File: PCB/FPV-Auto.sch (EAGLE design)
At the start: 93 parts, among them Q310 CSD25402Q3A, Q320 BSS138, U110 NRF24L01+_MINI, U120 74LVC2T45DCT, U140 DRV8835, U200 RASPBERRY_PI_ZERO_W_V1.1_GPIO, U210 MAX98357A, U300 BQ25892, U330 TPS61236P, U340 TPS61236P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

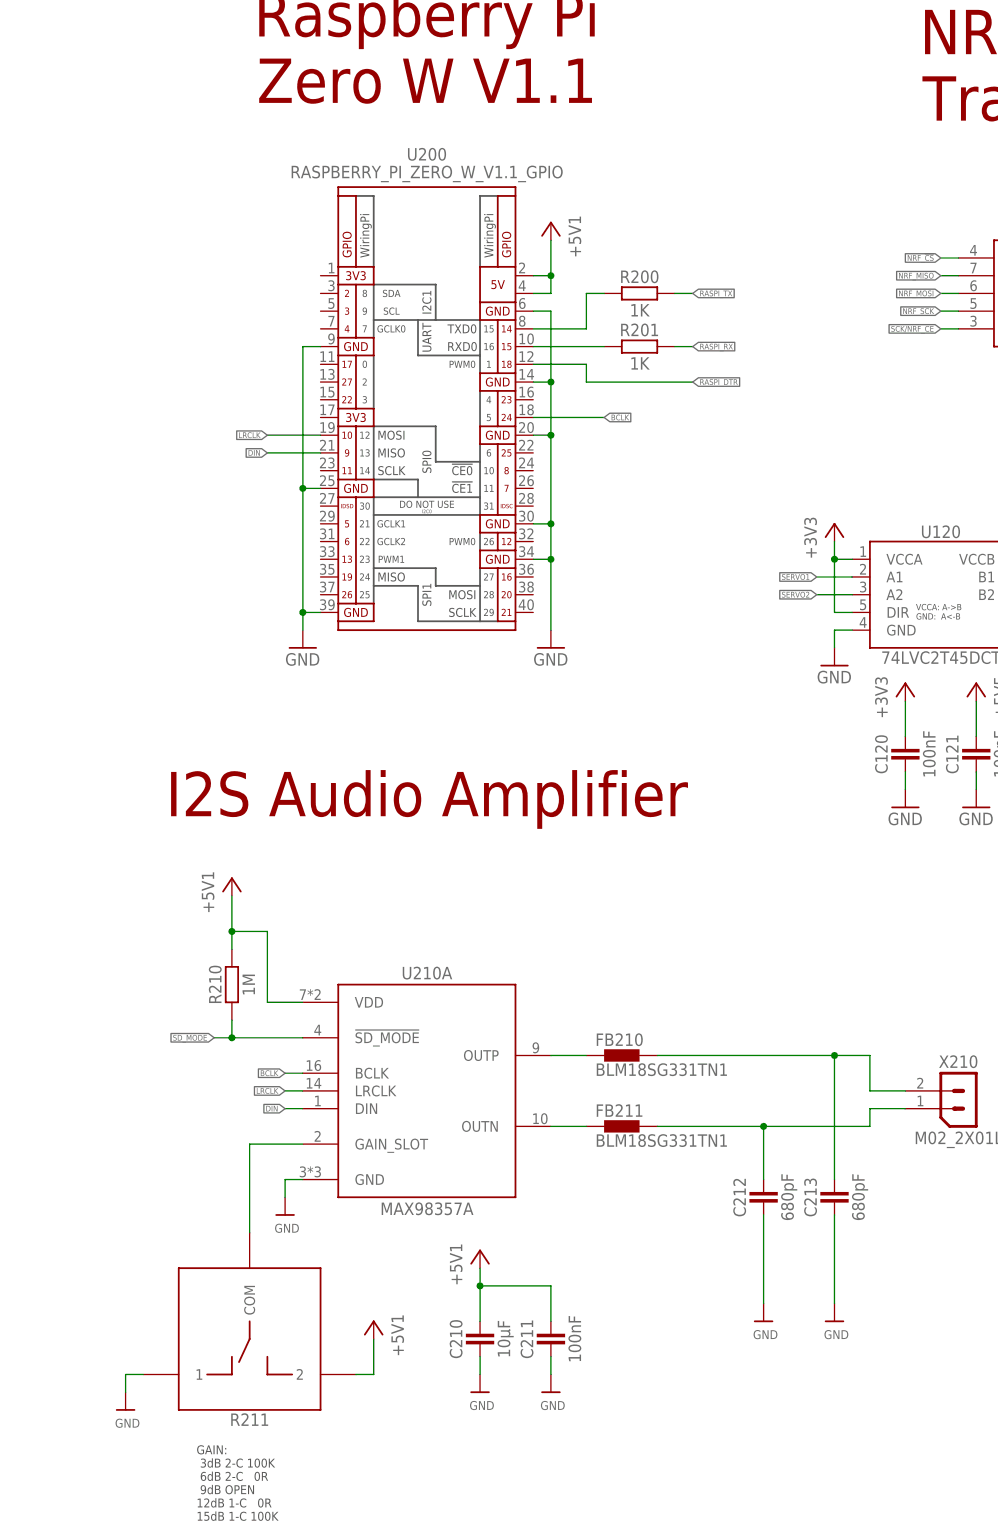
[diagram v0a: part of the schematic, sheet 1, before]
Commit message: Changes on Raspberry GPIO assignment
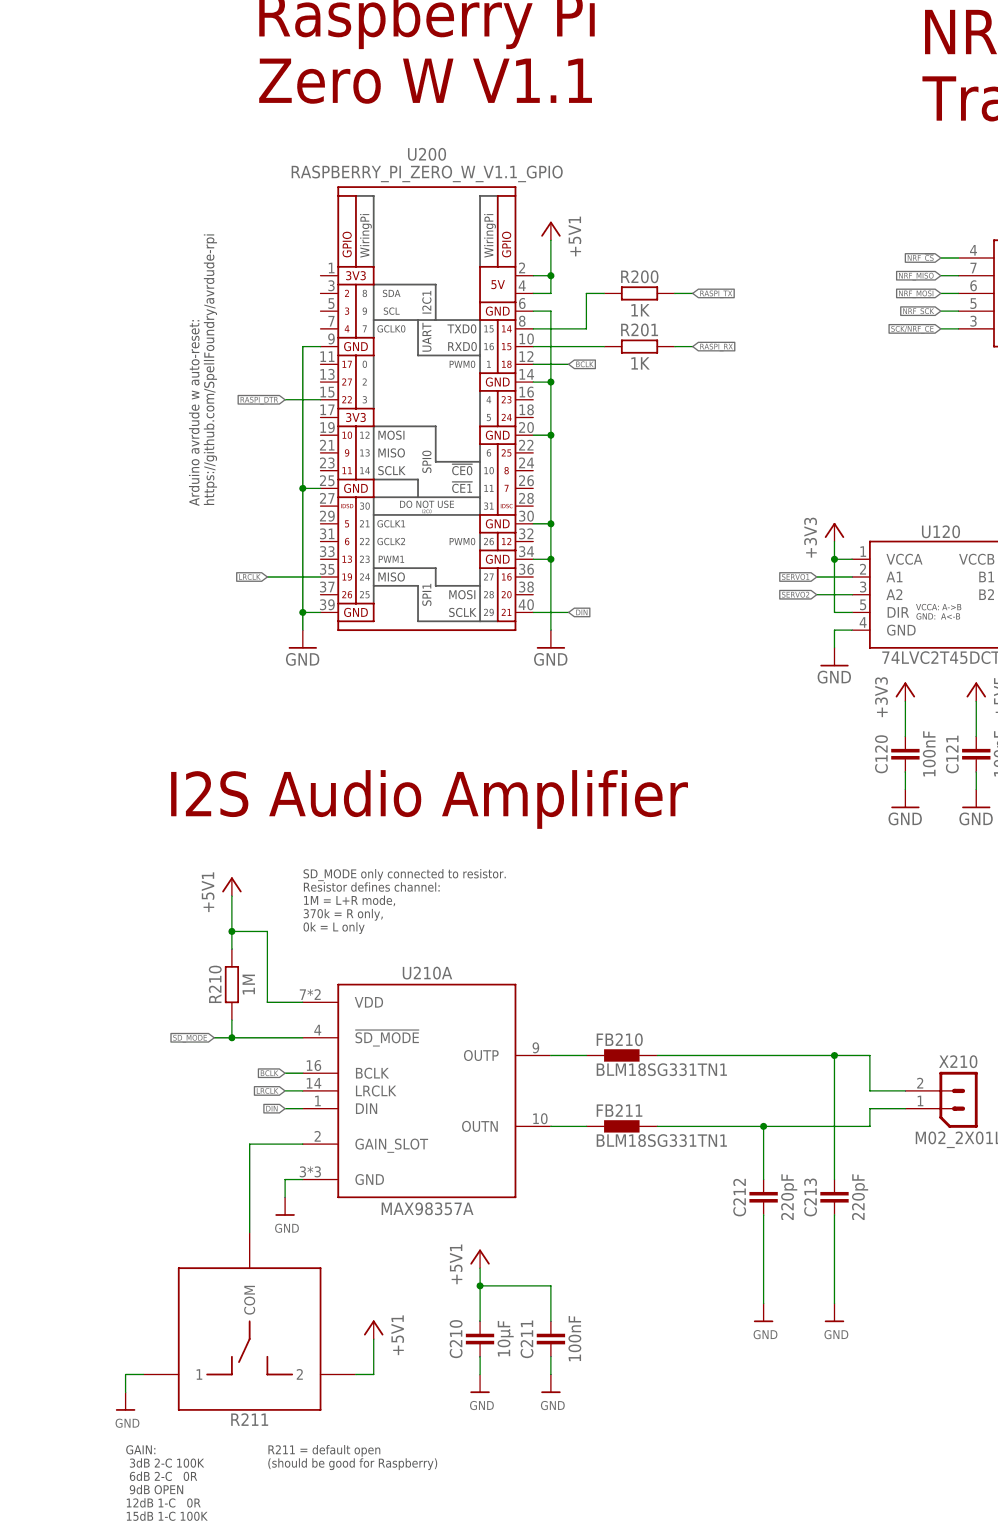
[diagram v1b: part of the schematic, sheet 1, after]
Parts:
- C212, C213: value 680pF -> 220pF
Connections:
- net BCLK: now also U200.GPIO18; no longer U200.GPIO24/GEN5
- net DIN: now also U200.GPIO21; no longer U200.GPIO9/MISO
- net LRCLK: now also U200.GPIO19; no longer U200.GPIO10/MOSI
- net RASPI_DTR: now also U200.GPIO22/GEN3; no longer U200.GPIO18
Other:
- note added: "Arduino avrdude w auto-reset: https://github.com/SpellFoundry/avrdude-rpi"
- note added: "DIN, BCLK, LRCLK was on wrong pins (was pin# instead GPIO#). Should be now: DIN=GPIO21, BLCK=GPIO18, LRCLK=GPIO19"
- note added: "R211 = default open (should be good for Raspberry)"
- note added: "SD_MODE only connected to resistor. Resistor defines channel: 1M = L+R mode, 370k = R only, 0k = L only"
- note added: "Yes please, this is better for antenna"
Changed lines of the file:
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@@
 <layer number="250" name="Descript" color="7" fill="1" visible="yes" active="yes"/>
 <layer number="251" name="SMDround" color="7" fill="1" visible="yes" active="yes"/>
-<layer number="254" name="Kommentar" color="7" fill="1" visible="yes" active="yes"/>
+<layer number="254" name="Kommentar" color="12" fill="1" visible="yes" active="yes"/>
 <layer number="255" name="HELP" color="7" fill="1" visible="yes" active="yes"/>
 </layers>
@@
 <part name="R200" library="FPV-Auto" deviceset="R" device="" value="1K"/>
 <part name="R201" library="FPV-Auto" deviceset="R" device="" value="1K"/>
-<part name="C212" library="FPV-Auto" deviceset="C" device="0603" value="680pF"/>
-<part name="C213" library="FPV-Auto" deviceset="C" device="0603" value="680pF"/>
+<part name="C212" library="FPV-Auto" deviceset="C" device="0603" value="220pF"/>
+<part name="C213" library="FPV-Auto" deviceset="C" device="0603" value="220pF"/>
 <part name="R211" library="FPV-Auto" deviceset="R_SWITCH_2_WAY" device="_0603" value="R_SWITCH_2_WAY_0603"/>
 <part name="+5V7" library="FPV-Auto" deviceset="+5V1" device=""/>
@@
 Zero W V1.1</text>
 <text x="101.6" y="228.6" size="6.35" layer="94" rot="R180" align="bottom-center">ATmega328/P</text>
-<text x="193.04" y="20.32" size="1.27" layer="97" align="top-left">GAIN:
+<text x="182.88" y="20.32" size="1.27" layer="97" align="top-left">GAIN:
  3dB 2-C 100K
  6dB 2-C   0R
@@
 <text x="166.116" y="152.654" size="1.778" layer="150" align="center-left">pin changed</text>
 <text x="166.116" y="139.954" size="1.778" layer="150" align="center-left">pin changed</text>
+<text x="195.58" y="127" size="1.27" layer="254">DIN, BCLK, LRCLK was on wrong pins (was pin# instead GPIO#).
+Should be now: DIN=GPIO21, BLCK=GPIO18, LRCLK=GPIO19</text>
+<text x="208.28" y="93.98" size="1.27" layer="97">SD_MODE only connected to resistor.
+Resistor defines channel:
+1M = L+R mode,
+370k = R only,
+0k = L only</text>
+<text x="203.2" y="20.32" size="1.27" layer="97" align="top-left">R211 = default open
+(should be good for Raspberry)</text>
+<text x="337.82" y="198.12" size="1.778" layer="254">Yes please, this is
+better for antenna </text>
+<text x="195.58" y="154.94" size="1.4224" layer="97" rot="R90">Arduino avrdude w auto-reset:
+https://github.com/SpellFoundry/avrdude-rpi</text>
 </plain>
 <instances>
@@
 </segment>
 <segment>
-<pinref part="U200" gate="GPIO" pin="GPIO24/GEN5"/>
-<wire x1="241.3" y1="167.64" x2="251.46" y2="167.64" width="0.1524" layer="91"/>
-<label x="251.46" y="167.64" size="0.8128" layer="95" xref="yes"/>
+<label x="246.38" y="175.26" size="0.8128" layer="95" xref="yes"/>
+<pinref part="U200" gate="GPIO" pin="GPIO18"/>
+<wire x1="246.38" y1="175.26" x2="241.3" y2="175.26" width="0.1524" layer="91"/>
 </segment>
 </net>
@@
 </segment>
 <segment>
-<pinref part="U200" gate="GPIO" pin="GPIO10/MOSI"/>
-<wire x1="210.82" y1="165.1" x2="203.2" y2="165.1" width="0.1524" layer="91"/>
-<label x="203.2" y="165.1" size="0.8128" layer="95" rot="R180" xref="yes"/>
+<label x="203.2" y="144.78" size="0.8128" layer="95" rot="R180" xref="yes"/>
+<pinref part="U200" gate="GPIO" pin="GPIO19"/>
+<wire x1="210.82" y1="144.78" x2="203.2" y2="144.78" width="0.1524" layer="91"/>
 </segment>
 </net>
@@
 </segment>
 <segment>
-<pinref part="U200" gate="GPIO" pin="GPIO9/MISO"/>
-<wire x1="210.82" y1="162.56" x2="203.2" y2="162.56" width="0.1524" layer="91"/>
-<label x="203.2" y="162.56" size="0.8128" layer="95" rot="R180" xref="yes"/>
+<label x="246.38" y="139.7" size="0.8128" layer="95" xref="yes"/>
+<pinref part="U200" gate="GPIO" pin="GPIO21"/>
+<wire x1="241.3" y1="139.7" x2="246.38" y2="139.7" width="0.1524" layer="91"/>
 </segment>
 </net>
@@
 <net name="RASPI_DTR" class="0">
 <segment>
-<pinref part="U200" gate="GPIO" pin="GPIO18"/>
-<wire x1="241.3" y1="175.26" x2="248.92" y2="175.26" width="0.1524" layer="91"/>
-<wire x1="248.92" y1="175.26" x2="248.92" y2="172.72" width="0.1524" layer="91"/>
-<wire x1="248.92" y1="172.72" x2="264.16" y2="172.72" width="0.1524" layer="91"/>
-<label x="264.16" y="172.72" size="0.8128" layer="95" xref="yes"/>
-</segment>
-<segment>
+<label x="205.74" y="170.18" size="0.8128" layer="95" rot="R180" xref="yes"/>
+<pinref part="U200" gate="GPIO" pin="GPIO22/GEN3"/>
+<wire x1="210.82" y1="170.18" x2="205.74" y2="170.18" width="0.1524" layer="91"/>
+</segment>
+<segment>

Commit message: Update PCB Layout
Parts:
- added R101: 10K, FPV-Auto:R
- added R103: 1K, FPV-Auto:R
- R102: value 10K -> 1K
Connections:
- net +3V3: now also R101.2, R103.2
- net RESET: now also R101.1; no longer R102.1
- net SCL: now also R103.1
- net SDA: now also R102.1
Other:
- note added: "pin 9 connected to GND"
- moved on the sheet: R102, U110
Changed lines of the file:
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@@
 <part name="+3V2" library="supply1" deviceset="+3V3" device=""/>
 <part name="+3V3" library="supply1" deviceset="+3V3" device=""/>
-<part name="R102" library="FPV-Auto" deviceset="R" device="" value="10K"/>
+<part name="R101" library="FPV-Auto" deviceset="R" device="" value="10K"/>
 <part name="C104" library="FPV-Auto" deviceset="C" device="0603" value="100nF"/>
 <part name="R304" library="FPV-Auto" deviceset="R" device="" value="30K1"/>
@@
 <part name="GND40" library="supply1" deviceset="GND" device=""/>
 <part name="GND41" library="supply1" deviceset="GND" device=""/>
+<part name="R103" library="FPV-Auto" deviceset="R" device="" value="1K"/>
+<part name="R102" library="FPV-Auto" deviceset="R" device="" value="1K"/>
+<part name="+3V4" library="supply1" deviceset="+3V3" device=""/>
 </parts>
 <sheets>
@@
 <text x="195.58" y="154.94" size="1.4224" layer="97" rot="R90">Arduino avrdude w auto-reset:
 https://github.com/SpellFoundry/avrdude-rpi</text>
+<text x="305.816" y="205.994" size="1.778" layer="150" align="center-left">pin 9 connected to GND</text>
 </plain>
 <instances>
@@
 <instance part="+3V2" gate="G$1" x="48.26" y="215.9"/>
 <instance part="+3V3" gate="G$1" x="17.78" y="208.28"/>
-<instance part="R102" gate="A" x="48.26" y="205.74" smashed="yes" rot="R90">
+<instance part="R101" gate="A" x="48.26" y="205.74" smashed="yes" rot="R90">
 <attribute name="NAME" x="46.7614" y="205.74" size="1.778" layer="95" font="vector" rot="R90" align="bottom-center"/>
 <attribute name="VALUE" x="49.784" y="205.74" size="1.778" layer="96" font="vector" rot="R90" align="top-center"/>
@@
 <instance part="C120" gate="A" x="294.64" y="119.38"/>
 <instance part="C121" gate="A" x="304.8" y="119.38"/>
+<instance part="R103" gate="A" x="175.26" y="195.58" smashed="yes" rot="R90">
+<attribute name="NAME" x="173.7614" y="195.58" size="1.778" layer="95" font="vector" rot="R90" align="bottom-center"/>
+<attribute name="VALUE" x="176.784" y="195.58" size="1.778" layer="96" font="vector" rot="R90" align="top-center"/>
+</instance>
+<instance part="R102" gate="A" x="167.64" y="195.58" smashed="yes" rot="R90">
+<attribute name="NAME" x="166.1414" y="195.58" size="1.778" layer="95" font="vector" rot="R90" align="bottom-center"/>
+<attribute name="VALUE" x="169.164" y="195.58" size="1.778" layer="96" font="vector" rot="R90" align="top-center"/>
+</instance>
+<instance part="+3V4" gate="G$1" x="175.26" y="210.82"/>
 </instances>
 <busses>
@@
 <wire x1="48.26" y1="213.36" x2="48.26" y2="210.82" width="0.1524" layer="91"/>
 <pinref part="+3V2" gate="G$1" pin="+3V3"/>
-<pinref part="R102" gate="A" pin="2"/>
+<pinref part="R101" gate="A" pin="2"/>
 </segment>
 <segment>
@@
 <wire x1="294.64" y1="121.92" x2="294.64" y2="127" width="0.1524" layer="91"/>
 </segment>
+<segment>
+<pinref part="R102" gate="A" pin="2"/>
+<wire x1="167.64" y1="200.66" x2="167.64" y2="203.2" width="0.1524" layer="91"/>
+<wire x1="167.64" y1="203.2" x2="175.26" y2="203.2" width="0.1524" layer="91"/>
+<pinref part="R103" gate="A" pin="2"/>
+<wire x1="175.26" y1="203.2" x2="175.26" y2="200.66" width="0.1524" layer="91"/>
+<pinref part="+3V4" gate="G$1" pin="+3V3"/>
+<wire x1="175.26" y1="203.2" x2="175.26" y2="208.28" width="0.1524" layer="91"/>
+<junction x="175.26" y="203.2"/>
+</segment>
 </net>
 <net name="MISO" class="0">
@@
 <junction x="43.18" y="198.12"/>
 <pinref part="C104" gate="A" pin="1"/>
-<pinref part="R102" gate="A" pin="1"/>
+<pinref part="R101" gate="A" pin="1"/>
 <pinref part="U100" gate="A" pin="PC6/!RESET!"/>
 </segment>
@@
 <segment>
 <pinref part="U100" gate="A" pin="PC4"/>
-<wire x1="149.86" y1="187.96" x2="152.4" y2="187.96" width="0.1524" layer="91"/>
-<label x="152.4" y="187.96" size="0.8128" layer="95" xref="yes"/>
+<wire x1="149.86" y1="187.96" x2="167.64" y2="187.96" width="0.1524" layer="91"/>
+<label x="177.8" y="187.96" size="0.8128" layer="95" xref="yes"/>
+<pinref part="R102" gate="A" pin="1"/>
+<wire x1="167.64" y1="187.96" x2="177.8" y2="187.96" width="0.1524" layer="91"/>
+<wire x1="167.64" y1="190.5" x2="167.64" y2="187.96" width="0.1524" layer="91"/>
+<junction x="167.64" y="187.96"/>
 </segment>
 </net>
@@
 <segment>
 <pinref part="U100" gate="A" pin="PC5"/>
-<wire x1="149.86" y1="185.42" x2="152.4" y2="185.42" width="0.1524" layer="91"/>
-<label x="152.4" y="185.42" size="0.8128" layer="95" xref="yes"/>
-</segment>
-</net>
+<wire x1="149.86" y1="185.42" x2="175.26" y2="185.42" width="0.1524" layer="91"/>
+<label x="177.8" y="185.42" size="0.8128" layer="95" xref="yes"/>
+<pinref part="R103" gate="A" pin="1"/>
+<wire x1="175.26" y1="185.42" x2="177.8" y2="185.42" width="0.1524" layer="91"/>
+<wire x1="175.26" y1="190.5" x2="175.26" y2="185.42" width="0.1524" layer="91"/>
+<junction x="175.26" y="185.42"/>
+</segment>
+</net>

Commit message: Z-Diode on reverse-prot-mosfet, button also on AVR, other minor changes
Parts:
- removed C310: (no value), FPV-Auto:C0603
- added D1: (no value), diode:ZENER-DIODESOD80C
- added R1, R2: 100K, FPV-Auto:R
- R102, R103: value 1K -> 10K
- R310: value 100K -> 10K
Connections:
- new net BUTTON_SENSE: R1.1, R2.2, U100A.ADC6
- new net N$15: D320.K1, R1.2
- net GND: now also R2.1; no longer C310.2
- net N$16: now also D1.A; no longer C310.1
- net VBUS: now also D1.C
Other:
- note added: "Add-on to detect button press after start-up"
- note added: "All pins checked - seems to be ok."
- note added: "Max. 14V"
- note added: "RASPI GPIO #22"
- note added: "Reset on power-up does not matter - all supplies held by button already."
- note added: "Unsere Namen hier irgendwo"
- note added: "Z-Diode mit 8-10V im SC79 bzw SOT523 package nehmen, z.B. https://www.mouser.de/datasheet/2/348/edzvfht2r9.1b-e-1493803.pdf Kondensator am Gate halte ich für Unsinn."
- note removed: "RASPI PIN 18/14"
- note removed: "choose filter C value"
- note removed: "pin changed"
- moved on the sheet: PAD_BAT+, PAD_BAT-, PAD_IN+, PAD_IN-

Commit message: updated lib and pcb
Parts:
- removed D1: (no value), diode:ZENER-DIODESOD80C
- removed R1, R2: 100K, FPV-Auto:R
- added D310: BZX585-B9V1, FPV-Auto:BZX585-B9V1
- added R322, R323: 100K, FPV-Auto:R
- U100: value (none) -> ATMEGA328P-AU; device FPV-Auto:ATMEGA328/P -> FPV-Auto:ATMEGA328P-AU
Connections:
- removed net NRF_MISO: U100A.PC3, U110.MISO
- removed net SCK/NRF_CE: U100A.PB5, U110.CE, X100.SCK
- new net NRF_CE: U100A.PC3, U110.CE
- new net SCK/NRF_MISO: U100A.PB5, U110.MISO, X100.SCK
- net BUTTON_SENSE: now also R322.1, R323.2, U100A.ADC7; no longer R1.1, R2.2, U100A.ADC6
- net GND: now also R323.1; no longer R2.1
- net N$15: now also R322.2; no longer R1.2
- net N$16: now also D310.A; no longer D1.A
- net NRF_!CS: now also U100A.PC2; no longer U100A.PC0
- net NRF_MOSI: now also U100A.PC0; no longer U100A.PC2
- net VBUS: now also D310.C; no longer D1.C
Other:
- note added: "changed pin"
- note added: "changed pin again, double check all"
- note added: "done"
- note added: "pin 9 connected to GND add polygon"
- note added: "stand so in deiner Vorlage"
- note removed: "pin 9 connected to GND"
- moved on the sheet: C100, C101, C102, C103, C104, C120, C121, C140, C141, C210, C211, C212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
